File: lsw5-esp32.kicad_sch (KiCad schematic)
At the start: 40 parts, among them J1 Conn_02x03_Odd_Even, J2 Conn_01x04_Pin, J3 USB4105-GF-A, J4 Conn_02x05_Odd_Even, J6 Conn_01x04, Q1 AO3407A, U1 ESP32-S3-WROOM-1U, U2 LD1117S33TR_SOT223, U3 ISO1410DWR

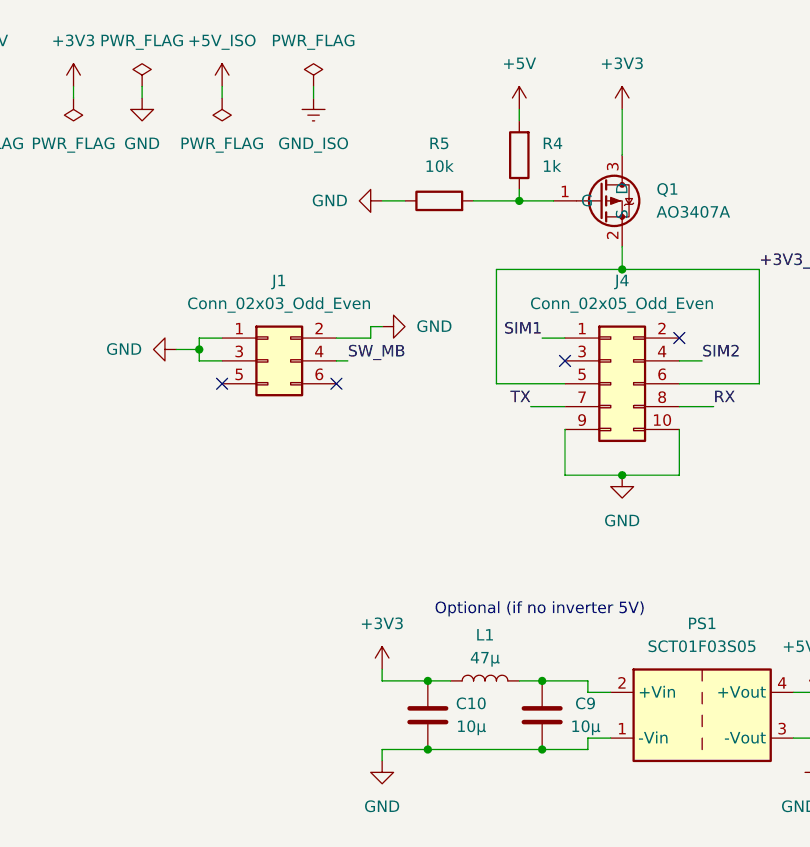
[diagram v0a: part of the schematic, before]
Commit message: fix some missed warnings
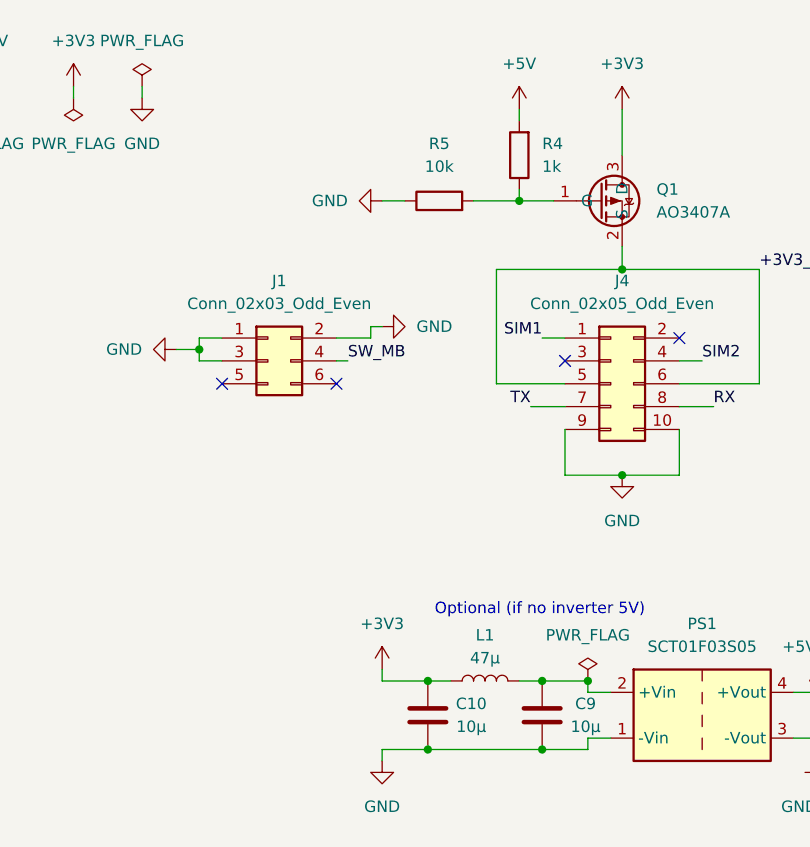
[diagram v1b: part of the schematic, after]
